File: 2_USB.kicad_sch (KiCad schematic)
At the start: 8 parts, among them J301 USB_C_Receptacle_USB2.0_16P, J302 Conn_02x03_Row_Letter_First, U301 CH224K, U302 FSUSB42MUX, U303 TPD2E001DRLR

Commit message: Add files via upload
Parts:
- U303: symbol TPD2E001DRLR:TPD2E01DRLR -> Polaris_symbols:TPD2E01DRLR
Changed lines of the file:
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@@
 	)
 	(symbol
-		(lib_id "TPD2E001DRLR:TPD2E01DRLR")
+		(lib_id "Polaris_symbols:TPD2E01DRLR")
 		(at 129.54 76.2 0)
 		(unit 1)

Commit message: Changed oscillator series resistors to DNP
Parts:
- D301: footprint (none) -> LED_SMD:LED_0603_1608Metric
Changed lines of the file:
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@@
 			)
 		)
-		(property "Footprint" ""
+		(property "Footprint" "LED_SMD:LED_0603_1608Metric"
 			(at 149.86 116.84 0)
 			(hide yes)

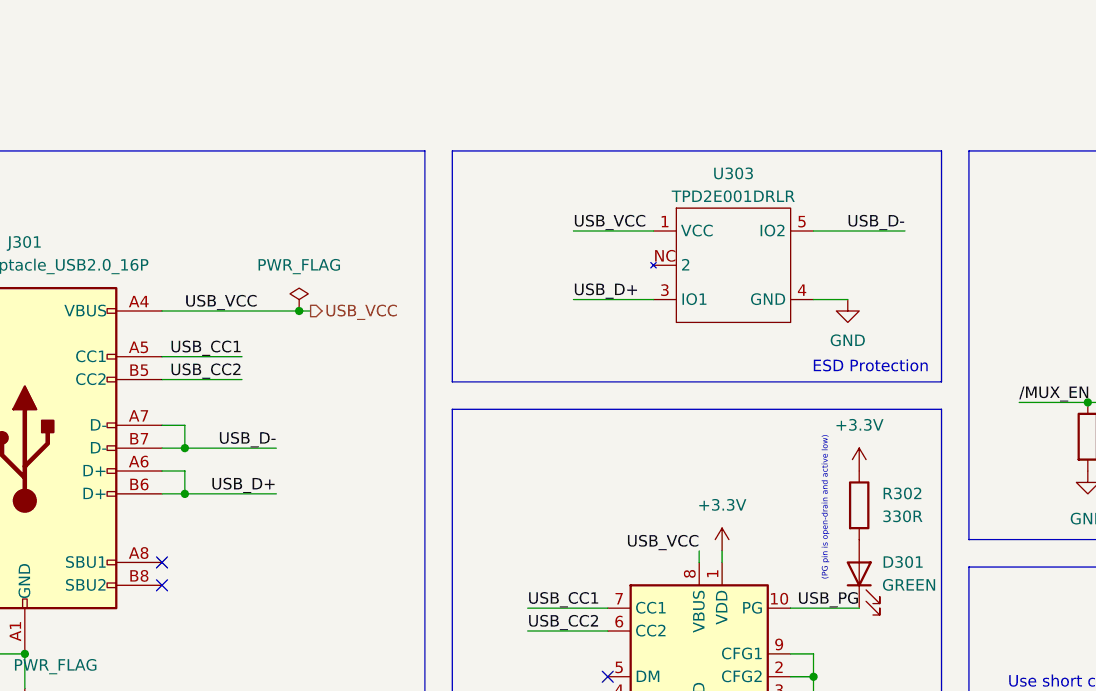
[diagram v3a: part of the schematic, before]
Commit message: Redid ESD protection because the previous chip couldn't handle 9V from USB-PD Finished status indication sections
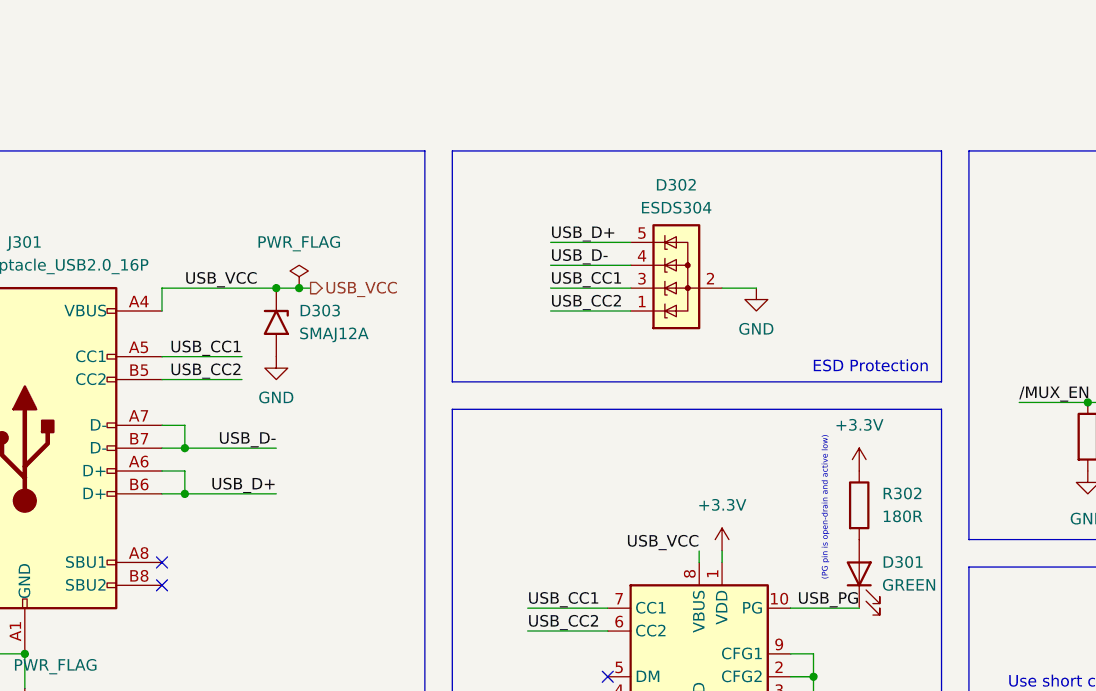
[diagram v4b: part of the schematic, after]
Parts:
- removed U303: TPD2E001DRLR, Package_TO_SOT_SMD:SOT-23-5, symbol Polaris_symbols:TPD2E01DRLR
- added D302: ESDS304, Package_TO_SOT_SMD:SOT-23-5, symbol Power_Protection:ESDS304
- added D303: SMAJ12A, Diode_SMD:D_SMA, symbol Diode:SMAJ12A
- R302: value 330R -> 180R
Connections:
- net GND: now also D302.2 (A), D303.2 (A2)
- net USB_CC1: now also D302.3 (K)
- net USB_CC2: now also D302.1 (K)
- net USB_D+: now also D302.5 (K)
- net USB_D-: now also D302.4 (K)
- net USB_VCC: now also D303.1 (A1)

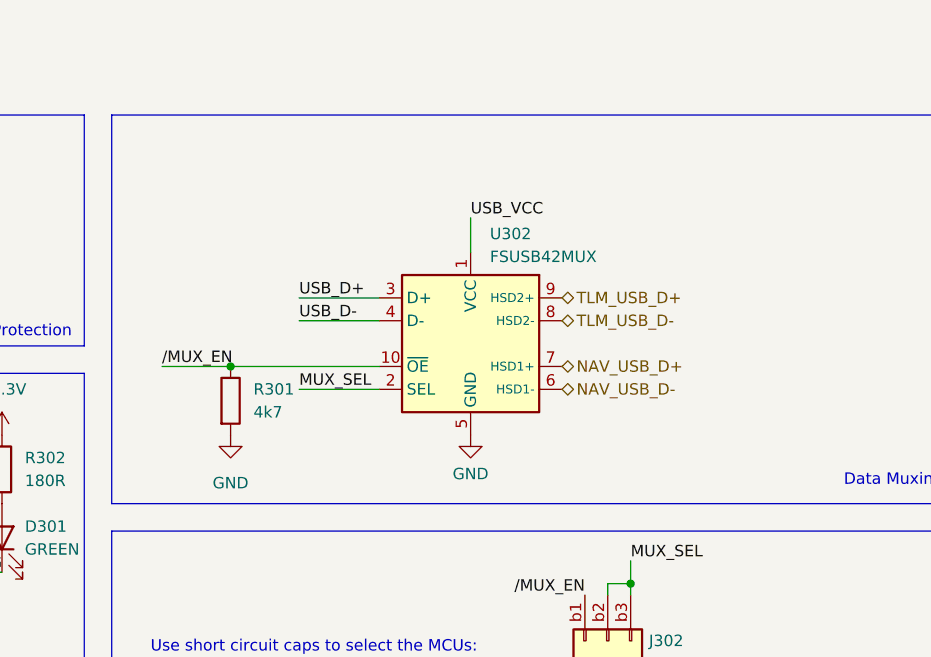
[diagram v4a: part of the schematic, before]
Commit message: Redid LoRa radio section Changed regulator output inductor to 10 uH based on availability
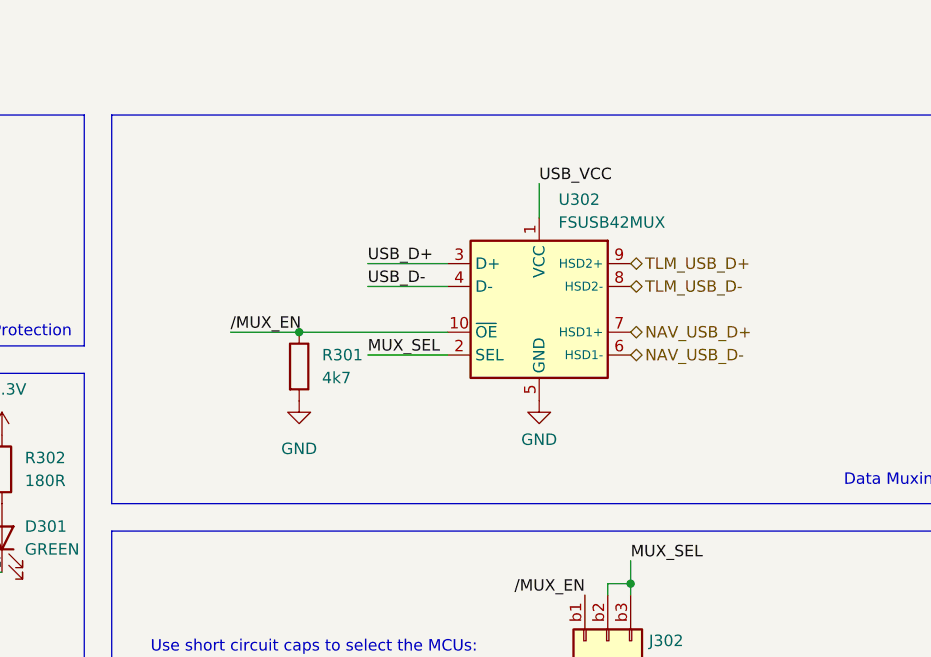
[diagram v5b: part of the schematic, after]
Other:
- moved on the sheet: R301, U302
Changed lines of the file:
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@@
 	)
 	(junction
-		(at 175.26 97.79)
+		(at 182.88 93.98)
 		(diameter 0)
 		(color 0 0 0 0)
@@
 	(wire
 		(pts
-			(xy 167.64 97.79) (xy 175.26 97.79)
+			(xy 175.26 93.98) (xy 182.88 93.98)
 		)
 		(stroke
@@
 	(wire
 		(pts
-			(xy 182.88 90.17) (xy 191.77 90.17)
+			(xy 190.5 86.36) (xy 199.39 86.36)
 		)
 		(stroke
@@
 	(wire
 		(pts
-			(xy 182.88 92.71) (xy 191.77 92.71)
+			(xy 190.5 88.9) (xy 199.39 88.9)
 		)
 		(stroke
@@
 	(wire
 		(pts
-			(xy 201.93 81.28) (xy 201.93 85.09)
+			(xy 209.55 77.47) (xy 209.55 81.28)
 		)
 		(stroke
@@
 	(wire
 		(pts
-			(xy 175.26 97.79) (xy 191.77 97.79)
+			(xy 182.88 93.98) (xy 199.39 93.98)
 		)
 		(stroke
@@
 	(wire
 		(pts
-			(xy 182.88 100.33) (xy 191.77 100.33)
+			(xy 190.5 96.52) (xy 199.39 96.52)
 		)
 		(stroke
@@
 	)
 	(label "USB_D+"
-		(at 182.88 90.17 0)
+		(at 190.5 86.36 0)
 		(effects
 			(font
@@
 	)
 	(label "USB_VCC"
-		(at 201.93 81.28 0)
+		(at 209.55 77.47 0)
 		(effects
 			(font
@@
 	)
 	(label "USB_D-"
-		(at 182.88 92.71 0)
+		(at 190.5 88.9 0)
 		(effects
 			(font
@@
 	)
 	(label "{slash}MUX_EN"
-		(at 167.64 97.79 0)
+		(at 175.26 93.98 0)
 		(effects
 			(font
@@
 	)
 	(label "MUX_SEL"
-		(at 182.88 100.33 0)
+		(at 190.5 96.52 0)
 		(effects
 			(font
@@
 	(hierarchical_label "NAV_USB_D-"
 		(shape bidirectional)
-		(at 212.09 100.33 0)
+		(at 219.71 96.52 0)
 		(effects
 			(font
@@
 	(hierarchical_label "TLM_USB_D-"
 		(shape bidirectional)
-		(at 212.09 92.71 0)
+		(at 219.71 88.9 0)
 		(effects
 			(font
@@
 	(hierarchical_label "NAV_USB_D+"
 		(shape bidirectional)
-		(at 212.09 97.79 0)
+		(at 219.71 93.98 0)
 		(effects
 			(font
@@
 	(hierarchical_label "TLM_USB_D+"
 		(shape bidirectional)
-		(at 212.09 90.17 0)
+		(at 219.71 86.36 0)
 		(effects
 			(font
@@
 	(symbol
 		(lib_id "Interface_USB:FSUSB42MUX")
-		(at 201.93 95.25 0)
+		(at 209.55 91.44 0)
 		(unit 1)
 		(body_style 1)
@@
 		(fields_autoplaced yes)
 		(property "Reference" "U302"
-			(at 204.0733 83.058 0)
+			(at 211.6933 79.248 0)
 			(show_name no)
 			(do_not_autoplace no)
@@
 		)
 		(property "Value" "FSUSB42MUX"
-			(at 204.0733 85.598 0)
+			(at 211.6933 81.788 0)
 			(show_name no)
 			(do_not_autoplace no)
@@
 		)
 		(property "Footprint" "Package_SO:MSOP-10_3x3mm_P0.5mm"
-			(at 201.93 115.57 0)
+			(at 209.55 111.76 0)
 			(hide yes)
 			(show_name no)
@@
 		)
 		(property "Datasheet" "https://www.onsemi.com/pub/Collateral/FSUSB42-D.PDF"
-			(at 201.93 97.79 0)
+			(at 209.55 93.98 0)
 			(hide yes)
 			(show_name no)
@@
 		)
 		(property "Description" "Low-Power, Two-Port, High-Speed, USB2.0 (480Mbps) or UART Switch, MSOP-10"
-			(at 201.93 95.25 0)
+			(at 209.55 91.44 0)
 			(hide yes)
 			(show_name no)
@@
 		)
 		(property "Description_1" ""
-			(at 201.93 95.25 0)
+			(at 209.55 91.44 0)
 			(hide yes)
 			(show_name no)
@@
 		)
 		(property "KLC_S3.3" ""
-			(at 201.93 95.25 0)
+			(at 209.55 91.44 0)
 			(hide yes)
 			(show_name no)
@@
 		)
 		(property "KLC_S4.1" ""
-			(at 201.93 95.25 0)
+			(at 209.55 91.44 0)
 			(hide yes)
 			(show_name no)
@@
 		)
 		(property "KLC_S4.2_DVDD" ""
-			(at 201.93 95.25 0)
+			(at 209.55 91.44 0)
 			(hide yes)
 			(show_name no)
@@
 		)
 		(property "KLC_S4.2_VREG_VOUT" ""
-			(at 201.93 95.25 0)
+			(at 209.55 91.44 0)
 			(hide yes)
 			(show_name no)
@@
 	(symbol
 		(lib_id "Device:R")
-		(at 175.26 101.6 0)
+		(at 182.88 97.79 0)
 		(unit 1)
 		(body_style 1)
@@
 		(fields_autoplaced yes)
 		(property "Reference" "R301"
-			(at 177.8 100.3299 0)
+			(at 185.42 96.5199 0)
 			(show_name no)
 			(do_not_autoplace no)
@@
 		)
 		(property "Value" "4k7"
-			(at 177.8 102.8699 0)
+			(at 185.42 99.0599 0)
 			(show_name no)
 			(do_not_autoplace no)
@@
 		)
 		(property "Footprint" "Resistor_SMD:R_0603_1608Metric"
-			(at 173.482 101.6 90)
+			(at 181.102 97.79 90)
 			(hide yes)
 			(show_name no)
@@
 		)
 		(property "Datasheet" ""
-			(at 175.26 101.6 0)
+			(at 182.88 97.79 0)
 			(hide yes)
 			(show_name no)
@@
 		)
 		(property "Description" "Resistor"
-			(at 175.26 101.6 0)
+			(at 182.88 97.79 0)
 			(hide yes)
 			(show_name no)
@@
 		)
 		(property "Description_1" ""
-			(at 175.26 101.6 0)
+			(at 182.88 97.79 0)
 			(hide yes)
 			(show_name no)
@@
 		)
 		(property "KLC_S3.3" ""
-			(at 175.26 101.6 0)
+			(at 182.88 97.79 0)
 			(hide yes)
 			(show_name no)
@@
 		)
 		(property "KLC_S4.1" ""
-			(at 175.26 101.6 0)
+			(at 182.88 97.79 0)
 			(hide yes)
 			(show_name no)
@@
 		)
 		(property "KLC_S4.2_DVDD" ""
-			(at 175.26 101.6 0)
+			(at 182.88 97.79 0)
 			(hide yes)
 			(show_name no)
@@
 		)
 		(property "KLC_S4.2_VREG_VOUT" ""
-			(at 175.26 101.6 0)
+			(at 182.88 97.79 0)
 			(hide yes)
 			(show_name no)
@@
 	(symbol
 		(lib_id "power:GND")
-		(at 201.93 105.41 0)
+		(at 209.55 101.6 0)
 		(unit 1)
 		(body_style 1)
@@
 		(fields_autoplaced yes)
 		(property "Reference" "#PWR0305"
-			(at 201.93 111.76 0)
+			(at 209.55 107.95 0)
 			(hide yes)
 			(show_name no)
@@
 		)
 		(property "Value" "GND"
-			(at 201.93 109.728 0)
+			(at 209.55 105.918 0)
 			(show_name no)
 			(do_not_autoplace no)
@@
 		)
 		(property "Footprint" ""
-			(at 201.93 105.41 0)
+			(at 209.55 101.6 0)
 			(hide yes)
 			(show_name no)
@@
 		)
 		(property "Datasheet" ""
-			(at 201.93 105.41 0)
+			(at 209.55 101.6 0)
 			(hide yes)
 			(show_name no)
@@
 		)
 		(property "Description" "Power symbol creates a global label with name \"GND\" , ground"
-			(at 201.93 105.41 0)
+			(at 209.55 101.6 0)
 			(hide yes)
 			(show_name no)
@@
 	(symbol
 		(lib_id "power:GND")
-		(at 175.26 105.41 0)
+		(at 182.88 101.6 0)
 		(unit 1)
 		(body_style 1)
@@
 		(fields_autoplaced yes)
 		(property "Reference" "#PWR0304"
-			(at 175.26 111.76 0)
+			(at 182.88 107.95 0)
 			(hide yes)
 			(show_name no)
@@
 		)
 		(property "Value" "GND"
-			(at 175.26 110.744 0)
+			(at 182.88 106.934 0)
 			(show_name no)
 			(do_not_autoplace no)
@@
 		)
 		(property "Footprint" ""
-			(at 175.26 105.41 0)
+			(at 182.88 101.6 0)
 			(hide yes)
 			(show_name no)
@@
 		)
 		(property "Datasheet" ""
-			(at 175.26 105.41 0)
+			(at 182.88 101.6 0)
 			(hide yes)
 			(show_name no)
@@
 		)
 		(property "Description" "Power symbol creates a global label with name \"GND\" , ground"
-			(at 175.26 105.41 0)
-			(hide yes)
-			(show_name no)
+			(at 182.88 101.6 0)
+			(hide yes)
+			(show_name no)
